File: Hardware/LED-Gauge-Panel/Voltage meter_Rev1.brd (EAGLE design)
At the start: 35 x 58.4 mm, 32 parts, among them J1 SL04, Q1 MOSFET-PCHANNEL, Q2 MOSFET-PCHANNEL, Q3 MOSFET-PCHANNEL, U1 ATMEGA328P_PDIPDIL28-4, U2 MAX232D, X1 22-23-2031, X2 16MHz

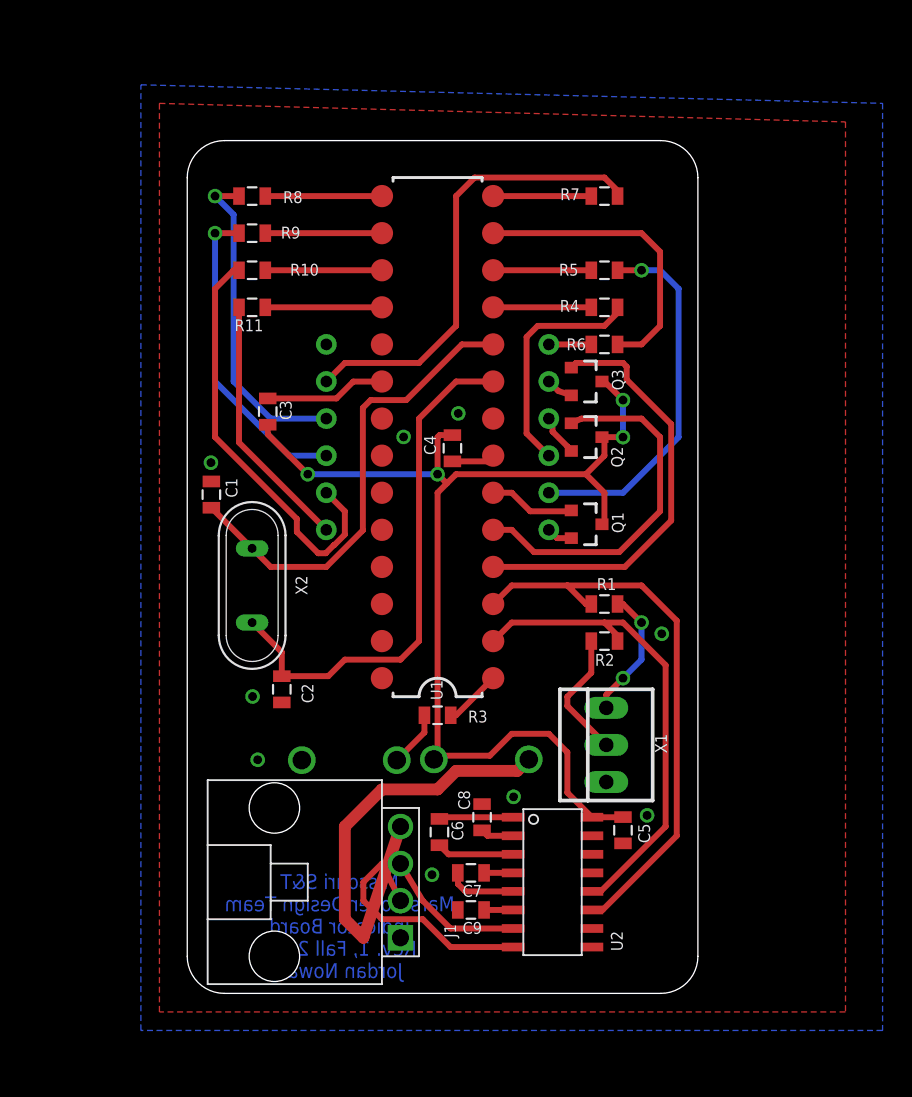
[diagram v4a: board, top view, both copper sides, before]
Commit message: Final edits to Indicator Board
Small corrections- Moved some vias, added mounting holes, adjusted
sides.
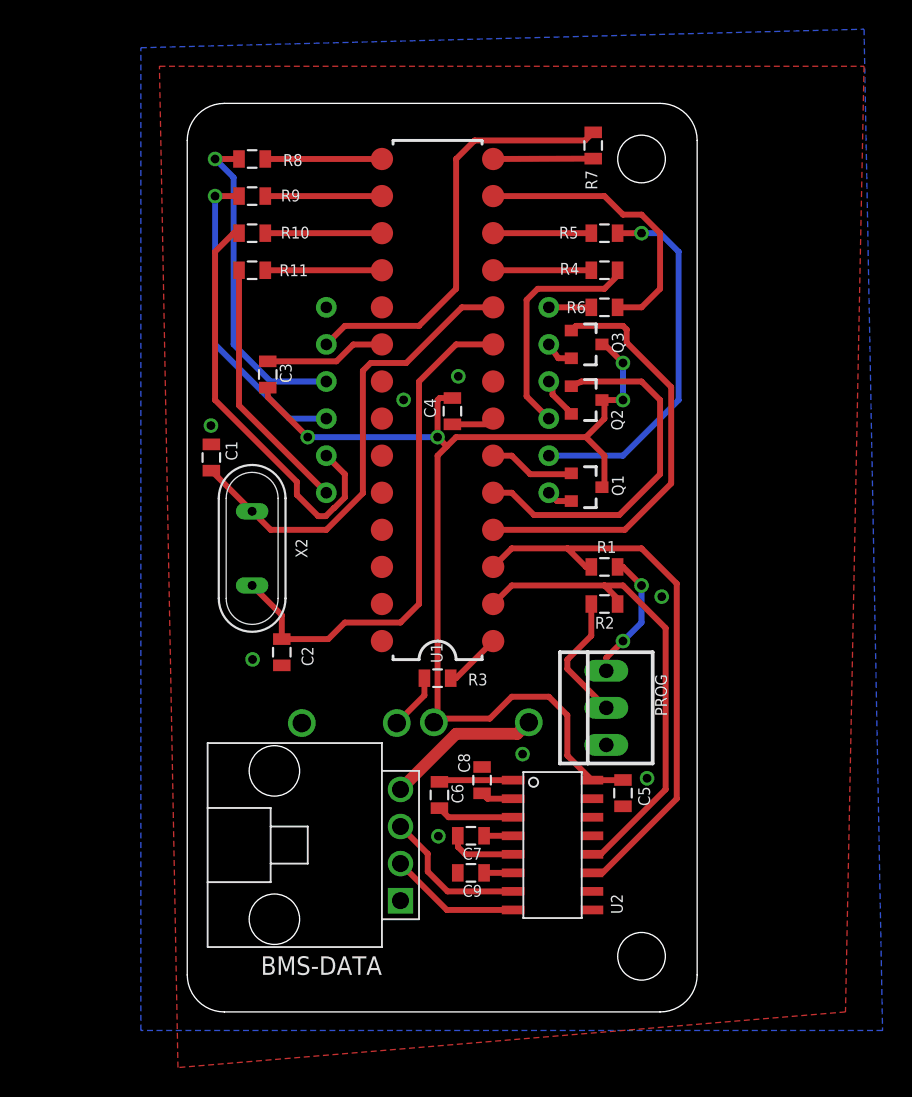
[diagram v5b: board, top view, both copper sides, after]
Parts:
- removed J1: SL04, MRDT-Connectors:MOLEX_SL_04_TH
- removed X1: 22-23-2031, con-molex:22-23-2031
- added BMS-DATA: SL04, MRDT-Connectors:MOLEX_SL_04_TH
- added H1, H4: MOUNTING_HOLE#4, MRDT-Hardware:#4_SCREW
- added PROG: 22-23-2031, con-molex:22-23-2031
- moved R7 3.55 mm to (29.7, 59.3), turned to 90 degrees
- moved C3 2.54 mm to (7.42, 43.7)
- moved C4 2.54 mm to (20.1, 41.1)
- moved R10 2.54 mm to (6.35, 53.3)
- moved R5 2.54 mm to (30.5, 53.3)
- moved C2 2.54 mm to (8.38, 24.6)
- moved R2 2.54 mm to (30.5, 27.9)
- moved C5 2.54 mm to (31.8, 15.0)
- moved C9 2.54 mm to (21.3, 9.53)
- moved C1 2.54 mm to (3.56, 38.0)
- moved C6 2.54 mm to (19.2, 14.9)
- moved C7 2.54 mm to (21.3, 12.1)
- moved C8 2.54 mm to (22.1, 15.9)
- moved LED1 2.54 mm to (19.1, 41.9)
- moved Q1 2.54 mm to (29.2, 35.9)
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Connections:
- net 232_RX: now also BMS-DATA.2; no longer J1.2
- net 232_TX: now also BMS-DATA.3; no longer J1.3
- net GND: now also BMS-DATA.1, PROG.1; no longer J1.1, X1.1
- net N$12: now also PROG.2; no longer X1.2
- net N$14: now also PROG.3; no longer X1.3
- net N$7: now also BMS-DATA.4; no longer J1.4
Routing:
- net N$7: track 30.7 -> 10.7 mm
- net 232_RX: track 17.5 -> 9.03 mm
- net G: track 31.7 -> 29.5 mm
- net N$18: track 20.5 -> 19.7 mm
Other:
- board size 35 x 58.4 mm -> 34.9 x 62.2 mm
- board text added: "POWER"
- board text added: "RESET"

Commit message: Added signiture
Last edit before ordering
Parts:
- added U$1: JORDAN-NOWAK, sig:JORDAN-NOWAK-SIG
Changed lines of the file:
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@@
 <element name="H1" library="MRDT-Hardware" package="#4_SCREW" value="MOUNTING_HOLE#4" x="33.02" y="58.42"/>
 <element name="H4" library="MRDT-Hardware" package="#4_SCREW" value="MOUNTING_HOLE#4" x="33.02" y="3.81"/>
+<element name="U$1" library="sig" package="JORDAN-NOWAK-SIG" value="JORDAN-NOWAK" x="21.59" y="2.54" rot="MR90"/>
 </elements>
 <signals>
